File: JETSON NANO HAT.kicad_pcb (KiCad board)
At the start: 2 copper layers, 24.4 x 65.3 mm, 12 parts, among them J1 CAMARRAY, J2 OUTPUTS, J4 INPUTS, P1 40 GPIO PINOUT

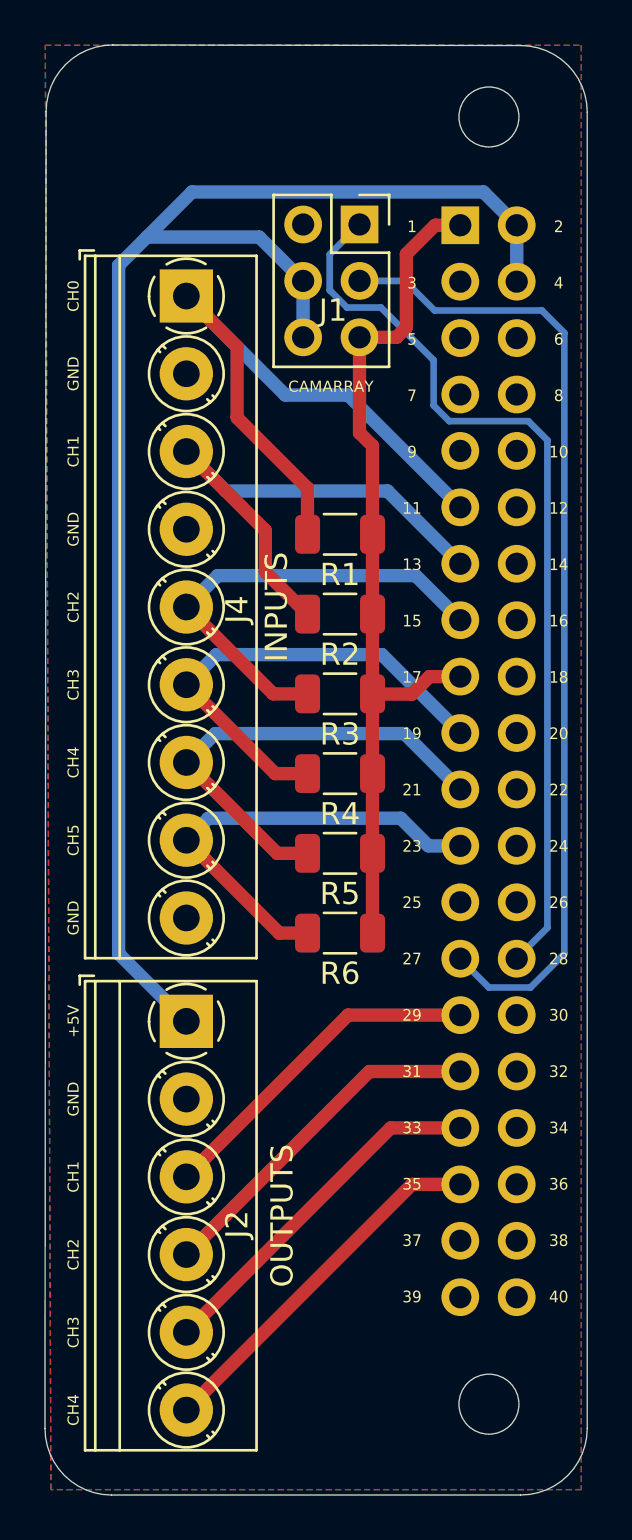
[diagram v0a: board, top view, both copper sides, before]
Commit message: new input added : 7 inputs 4 outputs & .sch - .pcb updated
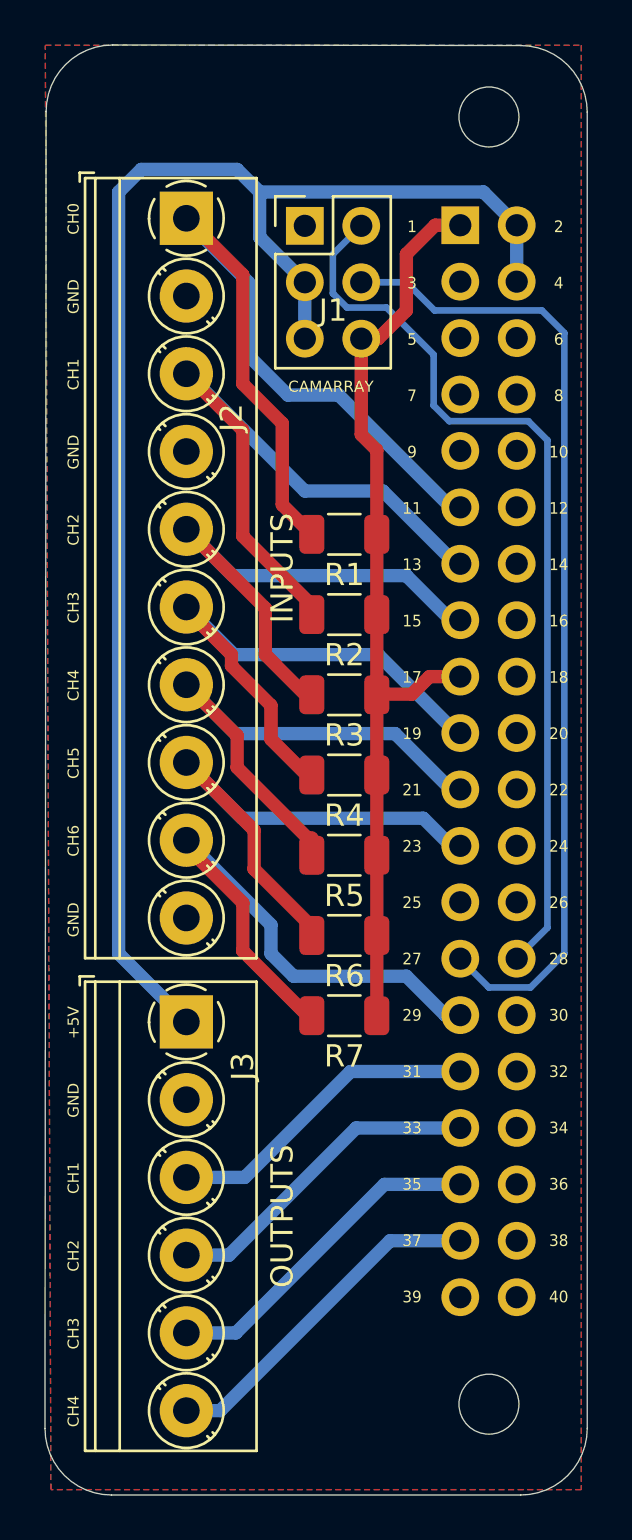
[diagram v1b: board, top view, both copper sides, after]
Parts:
- removed J4: INPUTS, TerminalBlock_Phoenix:TerminalBlock_Phoenix_PT-1,5-9-3.5-H_1x09_P3.50mm_Horizontal
- added J3: OUTPUTS, TerminalBlock_Phoenix:TerminalBlock_Phoenix_PT-1,5-6-3.5-H_1x06_P3.50mm_Horizontal, F.Cu at (111.3, 78.8)
- added R7: 1K ~ 10K, Resistor_SMD:R_1206_3216Metric, F.Cu at (118.4, 78.5)
- J1: footprint Connector_PinSocket_2.54mm:PinSocket_2x03_P2.54mm_Vertical -> Connector_PinHeader_2.54mm:PinHeader_2x03_P2.54mm_Vertical
- J2: value OUTPUTS -> INPUTS; footprint TerminalBlock_Phoenix:TerminalBlock_Phoenix_PT-1,5-6-3.5-H_1x06_P3.50mm_Horizontal -> TerminalBlock_Phoenix:TerminalBlock_Phoenix_PT-1,5-10-3.5-H_1x10_P3.50mm_Horizontal
- moved J2 36.2 mm to (111.3, 42.6)
- moved J1 2.46 mm to (116.6, 42.9)
- moved R6 0.22 mm to (118.4, 74.9)
- moved R5 0.21 mm to (118.4, 71.3)
- moved R4 0.20 mm to (118.4, 67.7)
- moved R3 0.20 mm to (118.4, 64.0)
- moved R2 0.19 mm to (118.4, 60.4)
- moved R1 0.19 mm to (118.4, 56.8)
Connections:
- J1 pad 1: SCL(CAMARRAY) -> GND
- J1 pad 2: GND -> SCL(CAMARRAY)
- J1 pad 3: SDA(CAMARRAY) -> +5V
- J1 pad 4: +5V -> SDA(CAMARRAY)
- J1 pad 5: +3.3V -> +5V
- J1 pad 6: +5V -> +3.3V
- J2 pad 1: +5V -> BTN_0.1
- J2 pad 3: GPIO6(GOOD) -> BTN_1.1
- J2 pad 4: GPIO7(WARNING) -> GND
- J2 pad 5: GPIO8(FAILURE) -> BTN_2.1
- J2 pad 6: GPIO9(EMPTY) -> BTN_3.1
- P1 pad 11: BTN0.1 -> BTN_0.1
- P1 pad 13: BTN1.1 -> BTN_1.1
- P1 pad 15: BTN2.1 -> BTN_2.1
- P1 pad 19: BTN3.1 -> BTN_3.1
- P1 pad 21: BTN4.1 -> BTN_4.1
- P1 pad 23: BTN5.1 -> BTN_5.1
- P1 pad 29: GPIO6(GOOD) -> BTN_6.1
- P1 pad 31: GPIO7(WARNING) -> GPIO_7
- P1 pad 33: GPIO8(FAILURE) -> GPIO_8
- P1 pad 35: GPIO9(EMPTY) -> GPIO_9
- P1 pad 37: /GPIO26 -> GPIO_10
- R1 pad 2: BTN0.1 -> BTN_0.1
- R2 pad 2: BTN1.1 -> BTN_1.1
- R3 pad 2: BTN2.1 -> BTN_2.1
- R4 pad 2: BTN3.1 -> BTN_3.1
- R5 pad 2: BTN4.1 -> BTN_4.1
- R6 pad 2: BTN5.1 -> BTN_5.1
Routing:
- net BTN_0.1: track 0.00 -> 36.3 mm
- net BTN0.1: track 29.3 -> 0.00 mm
- net BTN_1.1: track 0.00 -> 28.4 mm
- net BTN_6.1: track 0.00 -> 26.5 mm
- net BTN_3.1: track 0.00 -> 24.5 mm
- net BTN_4.1: track 0.00 -> 24.3 mm
- net BTN1.1: track 24.0 -> 0.00 mm
- net BTN_5.1: track 0.00 -> 23.9 mm
- net BTN_2.1: track 0.00 -> 23.8 mm
- net BTN3.1: track 21.5 -> 0.00 mm
- net BTN4.1: track 21.1 -> 0.00 mm
- net BTN2.1: track 20.8 -> 0.00 mm
- net BTN5.1: track 20.4 -> 0.00 mm
- net GPIO9(EMPTY): track 16.5 -> 0.00 mm
- net GPIO8(FAILURE): track 16.1 -> 0.00 mm
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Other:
- board text added: "CH6"
